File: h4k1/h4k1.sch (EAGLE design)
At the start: 202 parts, among them IC1 STM32F10XCXT6, J2 PJ-313D-AUDIO-JACK, J3 USB-AF10, K1 CHERRY-MX-LED, K10 CHERRY-MX, K11 CHERRY-MX, K12 CHERRY-MX, K13 CHERRY-MX, K14 CHERRY-MX, K15 CHERRY-MX, K16 CHERRY-MX, K17 CHERRY-MX-LED, K18 CHERRY-MX, K19 CHERRY-MX, K2 CHERRY-MX-LED, K20 CHERRY-MX, K21 CHERRY-MX, K22 CHERRY-MX, K23 CHERRY-MX, K24 CHERRY-MX, K25 CHERRY-MX-LED, K26 CHERRY-MX, K27 CHERRY-MX, K28 CHERRY-MX, K29 CHERRY-MX, K3 CHERRY-MX-LED, K30 CHERRY-MX, K31 CHERRY-MX, K32 CHERRY-MX, K33 CHERRY-MX-LED, K34 CHERRY-MX, K35 CHERRY-MX, K36 CHERRY-MX-LED, K37 CHERRY-MX-LED, K38 CHERRY-MX, K39 CHERRY-MX, K4 CHERRY-MX-LED, K40 CHERRY-MX-LED, K41 CHERRY-MX, K42 CHERRY-MX, K43 CHERRY-MX, K44 CHERRY-MX, K45 CHERRY-MX, K46 CHERRY-MX-LED, K5 CHERRY-MX-LED, K6 CHERRY-MX-LED, K65 EVQPUL02K, K66 EVQPUL02K, K67 K3-1280S-F2, K7 CHERRY-MX-LED, K8 CHERRY-MX-LED, K9 CHERRY-MX-LED, T1 DBG, U1 GL850G, U3 PCM2704CDB, U4 74HC138, X3 12MHz, X4 12MHz

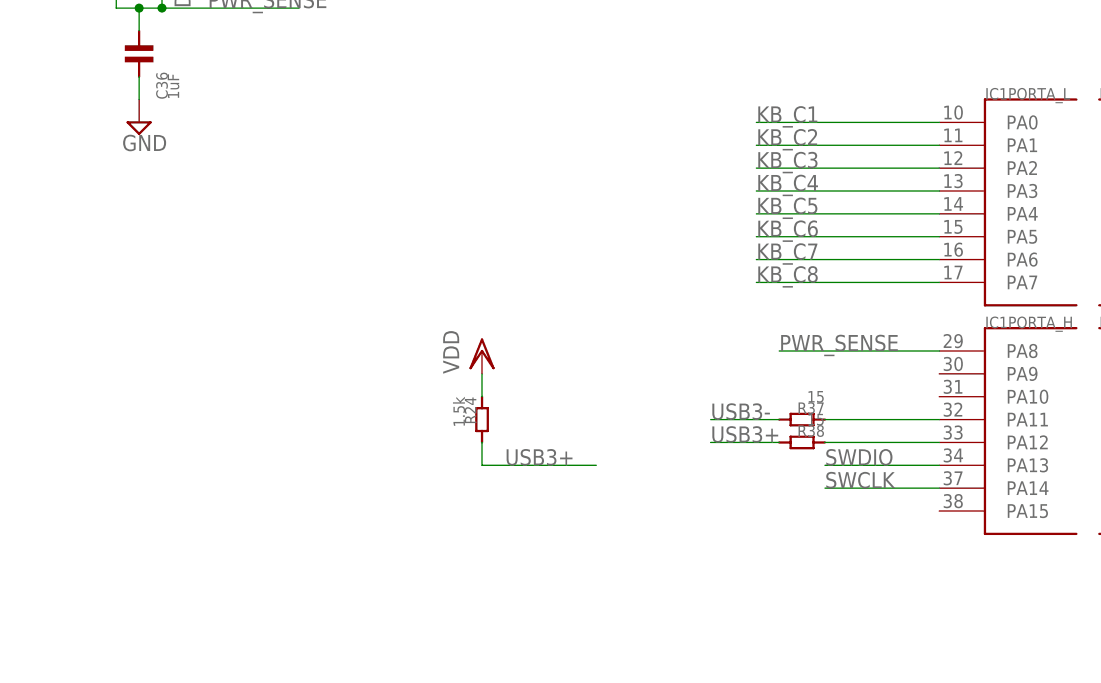
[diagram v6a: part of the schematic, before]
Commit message: add usb disconnect pin
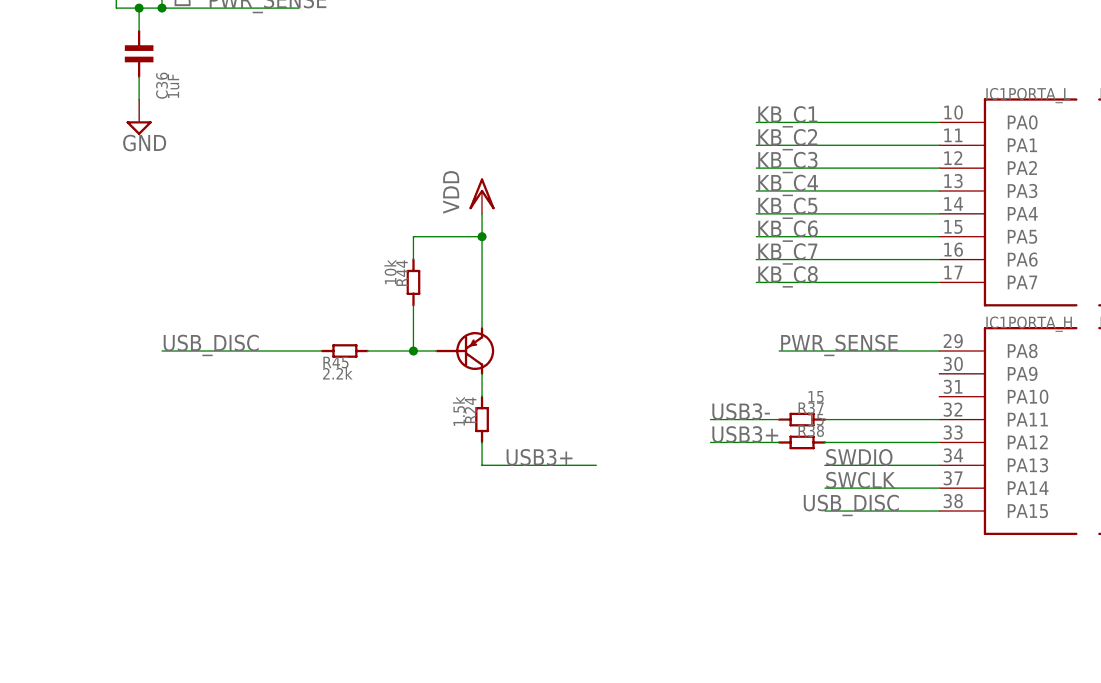
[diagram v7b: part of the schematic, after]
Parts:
- added R44: 10k, hqc:R-0805
- added R45: 2.2k, hqc:R-0805
- added U5: SS8550-SOT-323, hqc:SS8550-SOT-323
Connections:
- new net N$87: R44.P$2, R45.P$2, U5.P$B
- new net N$91: R24.P$1, U5.P$C
- new net USB_DISC: IC1PORTA_H.PA15, R45.P$1
- net VDD: now also R44.P$1, U5.P$E; no longer R24.P$1
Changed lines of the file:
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@@
 <part name="SUPPLY32" library="supply2" deviceset="GND" device=""/>
 <part name="D51" library="hqc-basic" deviceset="IN4148WS-SWITCHING-DIODE" device=""/>
+<part name="U5" library="hqc" deviceset="SS8550-SOT-323" device=""/>
+<part name="R44" library="hqc" deviceset="R-0805" device="" value="10k"/>
+<part name="R45" library="hqc" deviceset="R-0805" device="" value="2.2k"/>
 </parts>
 <sheets>
@@
 <instance part="U$7" gate="G$1" x="647.7" y="-127"/>
 <instance part="U$8" gate="G$1" x="627.38" y="-127"/>
-<instance part="VDD18" gate="G$1" x="-12.7" y="45.72"/>
+<instance part="VDD18" gate="G$1" x="-12.7" y="63.5"/>
 <instance part="R24" gate="G$1" x="-12.7" y="38.1" rot="R270"/>
 <instance part="U4" gate="74HC138" x="-43.18" y="-147.32"/>
@@
 <instance part="SUPPLY32" gate="GND" x="-50.8" y="71.12"/>
 <instance part="D51" gate="G$1" x="-48.26" y="88.9" rot="R90"/>
+<instance part="U5" gate="G$1" x="-15.24" y="45.72"/>
+<instance part="R44" gate="G$1" x="-20.32" y="53.34" rot="R270"/>
+<instance part="R45" gate="G$1" x="-27.94" y="45.72"/>
 </instances>
 <busses>
@@
 </segment>
 <segment>
-<pinref part="VDD18" gate="G$1" pin="VDD"/>
-<pinref part="R24" gate="G$1" pin="P$1"/>
-<wire x1="-12.7" y1="43.18" x2="-12.7" y2="40.64" width="0.1524" layer="91"/>
-</segment>
-<segment>
 <pinref part="U4" gate="74HC138" pin="VCC"/>
 <wire x1="-58.42" y1="-134.62" x2="-63.5" y2="-134.62" width="0.1524" layer="91"/>
@@
 <pinref part="D51" gate="G$1" pin="P$2"/>
 <wire x1="-48.26" y1="91.44" x2="-48.26" y2="93.98" width="0.1524" layer="91"/>
+</segment>
+<segment>
+<pinref part="VDD18" gate="G$1" pin="VDD"/>
+<pinref part="U5" gate="G$1" pin="P$E"/>
+<wire x1="-12.7" y1="60.96" x2="-12.7" y2="58.42" width="0.1524" layer="91"/>
+<pinref part="R44" gate="G$1" pin="P$1"/>
+<wire x1="-12.7" y1="58.42" x2="-12.7" y2="48.26" width="0.1524" layer="91"/>
+<wire x1="-20.32" y1="55.88" x2="-20.32" y2="58.42" width="0.1524" layer="91"/>
+<wire x1="-20.32" y1="58.42" x2="-12.7" y2="58.42" width="0.1524" layer="91"/>
+<junction x="-12.7" y="58.42"/>
 </segment>
 </net>
@@
 </segment>
 </net>
+<net name="N$87" class="0">
+<segment>
+<pinref part="U5" gate="G$1" pin="P$B"/>
+<pinref part="R45" gate="G$1" pin="P$2"/>
+<wire x1="-17.78" y1="45.72" x2="-20.32" y2="45.72" width="0.1524" layer="91"/>
+<pinref part="R44" gate="G$1" pin="P$2"/>
+<wire x1="-20.32" y1="45.72" x2="-25.4" y2="45.72" width="0.1524" layer="91"/>
+<wire x1="-20.32" y1="50.8" x2="-20.32" y2="45.72" width="0.1524" layer="91"/>
+<junction x="-20.32" y="45.72"/>
+</segment>
+</net>
+<net name="USB_DISC" class="0">
+<segment>
+<pinref part="R45" gate="G$1" pin="P$1"/>
+<wire x1="-30.48" y1="45.72" x2="-48.26" y2="45.72" width="0.1524" layer="91"/>
+<label x="-48.26" y="45.72" size="1.778" layer="95"/>
+</segment>
+<segment>
+<pinref part="IC1" gate="PORTA_H" pin="PA15"/>
+<wire x1="38.1" y1="27.94" x2="25.4" y2="27.94" width="0.1524" layer="91"/>
+<label x="22.86" y="27.94" size="1.778" layer="95"/>
+</segment>
+</net>
+<net name="N$91" class="0">
+<segment>
+<pinref part="R24" gate="G$1" pin="P$1"/>
+<pinref part="U5" gate="G$1" pin="P$C"/>
+<wire x1="-12.7" y1="40.64" x2="-12.7" y2="43.18" width="0.1524" layer="91"/>
+</segment>
+</net>
